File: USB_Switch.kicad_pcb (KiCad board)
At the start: 2 copper layers, 42 x 61 mm, 30 parts, among them J1 Conn_01x06, J2 USB_IN, J3 USB_OUT, J4 Conn_01x08, J5 USB_OUT, Q1 Q_NMOS_GDS, Q2 Q_NMOS_GDS, SW1 PRGM, U1 AMS1117-3.3, U2 INA219AxD, U3 INA219AxD, U4 ESP-12F

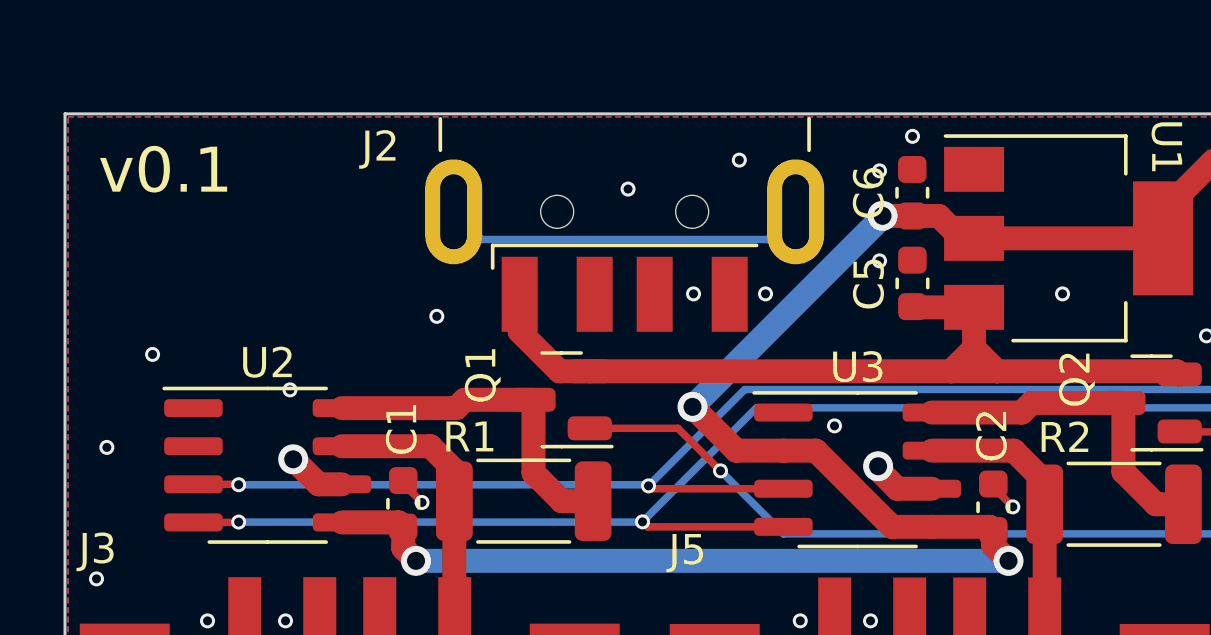
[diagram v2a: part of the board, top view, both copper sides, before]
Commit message: More GND via placements
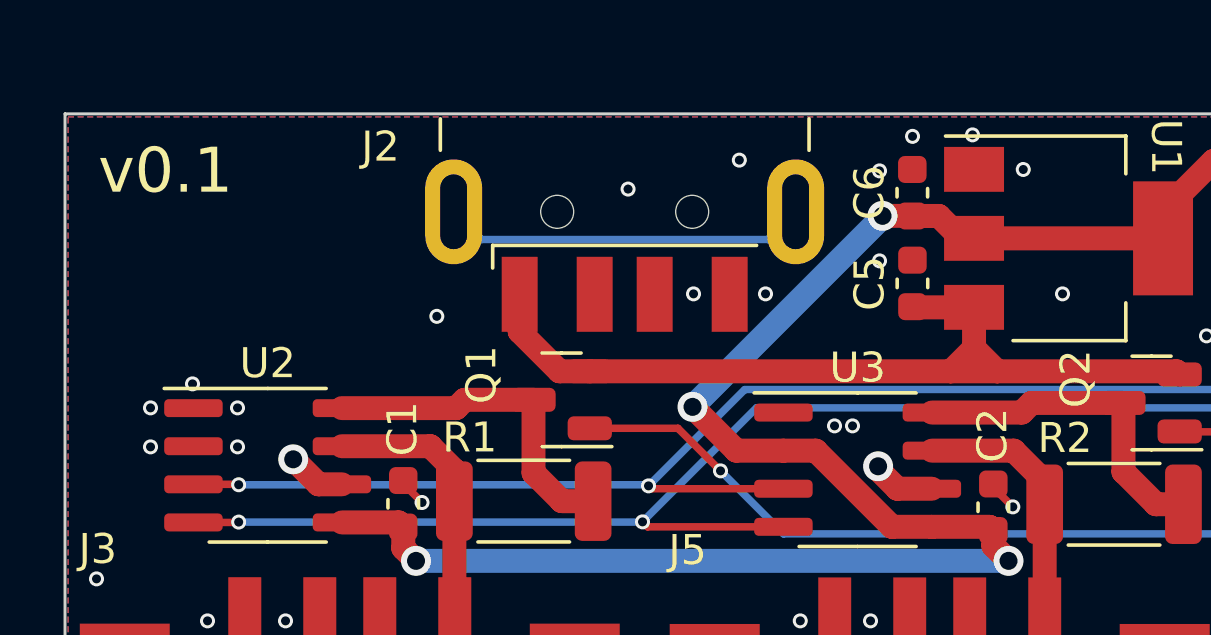
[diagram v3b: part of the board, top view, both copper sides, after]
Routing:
- net GND: vias 54 -> 59
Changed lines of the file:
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@@
   (via (at 73.5836 89.7304) (size 0.5) (drill 0.3) (layers "F.Cu" "B.Cu") (free) (net 27))
   (via (at 64.518794 128.501606) (size 0.5) (drill 0.3) (layers "F.Cu" "B.Cu") (free) (net 27))
+  (via (at 67.47544 84.184229) (size 0.5) (drill 0.3) (layers "F.Cu" "B.Cu") (free) (net 27))
   (via (at 59.3836 120.0304) (size 0.5) (drill 0.3) (layers "F.Cu" "B.Cu") (free) (net 27))
   (via (at 47.9266 89.0796) (size 0.5) (drill 0.3) (layers "F.Cu" "B.Cu") (free) (net 27))
@@
   (via (at 68.518794 117.451606) (size 0.5) (drill 0.3) (layers "F.Cu" "B.Cu") (free) (net 27))
   (via (at 54.302 84.8378) (size 0.5) (drill 0.3) (layers "F.Cu" "B.Cu") (free) (net 27))
-  (via (at 38.4524 90.3496) (size 0.5) (drill 0.3) (layers "F.Cu" "B.Cu") (free) (net 27))
+  (via (at 39.7836 91.3304) (size 0.5) (drill 0.3) (layers "F.Cu" "B.Cu") (free) (net 27))
   (via (at 49.268794 131.401606) (size 0.5) (drill 0.3) (layers "F.Cu" "B.Cu") (free) (net 27))
+  (via (at 65.7836 83.0304) (size 0.5) (drill 0.3) (layers "F.Cu" "B.Cu") (free) (net 27))
   (via (at 58.318794 140.251606) (size 0.5) (drill 0.3) (layers "F.Cu" "B.Cu") (free) (net 27))
   (via (at 62.6836 84.2304) (size 0.5) (drill 0.3) (layers "F.Cu" "B.Cu") (free) (net 27))
   (via (at 58.0104 83.8726) (size 0.5) (drill 0.3) (layers "F.Cu" "B.Cu") (free) (net 27))
+  (via (at 61.7836 92.7304) (size 0.5) (drill 0.3) (layers "F.Cu" "B.Cu") (free) (net 27))
+  (via (at 38.3836 93.4304) (size 0.5) (drill 0.3) (layers "F.Cu" "B.Cu") (free) (net 27))
   (via (at 62.3836 99.2304) (size 0.5) (drill 0.3) (layers "F.Cu" "B.Cu") (free) (net 27))
   (via (at 73.268794 123.451606) (size 0.5) (drill 0.3) (layers "F.Cu" "B.Cu") (free) (net 27))
@@
   (via (at 42.8836 99.2304) (size 0.5) (drill 0.3) (layers "F.Cu" "B.Cu") (free) (net 27))
   (via (at 62.636064 94.077936) (size 1) (drill 0.6) (layers "F.Cu" "B.Cu") (net 27))
-  (via (at 43.0336 91.5304) (size 0.5) (drill 0.3) (layers "F.Cu" "B.Cu") (free) (net 27))
+  (via (at 41.2836 92.1304) (size 0.5) (drill 0.3) (layers "F.Cu" "B.Cu") (free) (net 27))
   (via (at 51.968794 126.051606) (size 0.5) (drill 0.3) (layers "F.Cu" "B.Cu") (free) (net 27))
   (via (at 64.868794 114.401606) (size 0.5) (drill 0.3) (layers "F.Cu" "B.Cu") (free) (net 27))
@@
   (via (at 45.018794 127.001606) (size 0.5) (drill 0.3) (layers "F.Cu" "B.Cu") (free) (net 27))
   (via (at 66.818794 142.051606) (size 0.5) (drill 0.3) (layers "F.Cu" "B.Cu") (free) (net 27))
-  (via (at 36.9284 93.4484) (size 0.5) (drill 0.3) (layers "F.Cu" "B.Cu") (free) (net 27))
+  (via (at 38.3836 92.1304) (size 0.5) (drill 0.3) (layers "F.Cu" "B.Cu") (free) (net 27))
+  (via (at 41.2836 93.4304) (size 0.5) (drill 0.3) (layers "F.Cu" "B.Cu") (free) (net 27))
   (via (at 61.1836 92.7304) (size 0.5) (drill 0.3) (layers "F.Cu" "B.Cu") (free) (net 27))
   (via (at 52.718794 140.351606) (size 0.5) (drill 0.3) (layers "F.Cu" "B.Cu") (free) (net 27))
